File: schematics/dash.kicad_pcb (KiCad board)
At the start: 2 copper layers, 50 x 30 mm, 30 parts, among them J1 BATT_CONN, J2 EXTERNAL_TRIGGER, J3 USB_OTG, SW1 SW_Push, U1 ESP-12E, U2 ch340g, U3 MCP73833, U4 HT7333, Y1 12Mhz

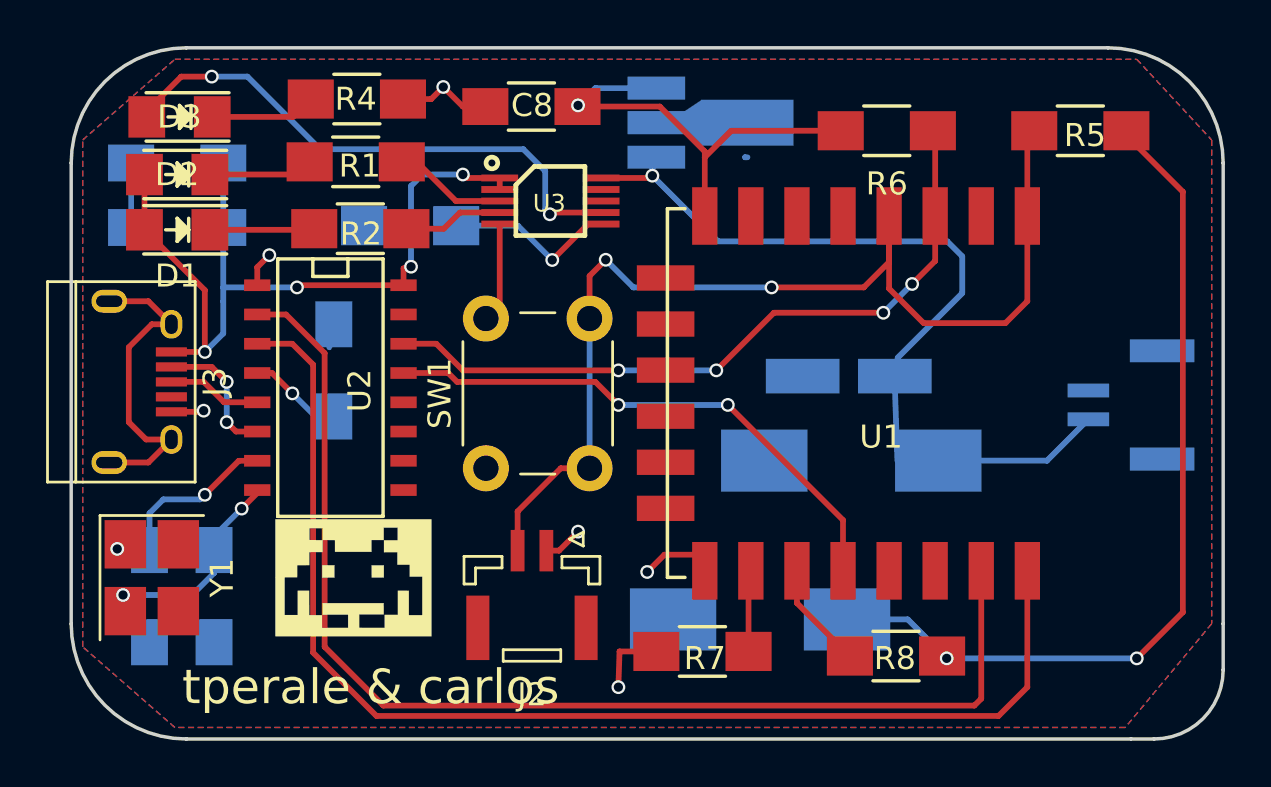
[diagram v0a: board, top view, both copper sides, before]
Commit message: [fix] Global dependencies to local dependencies (no more path problem)
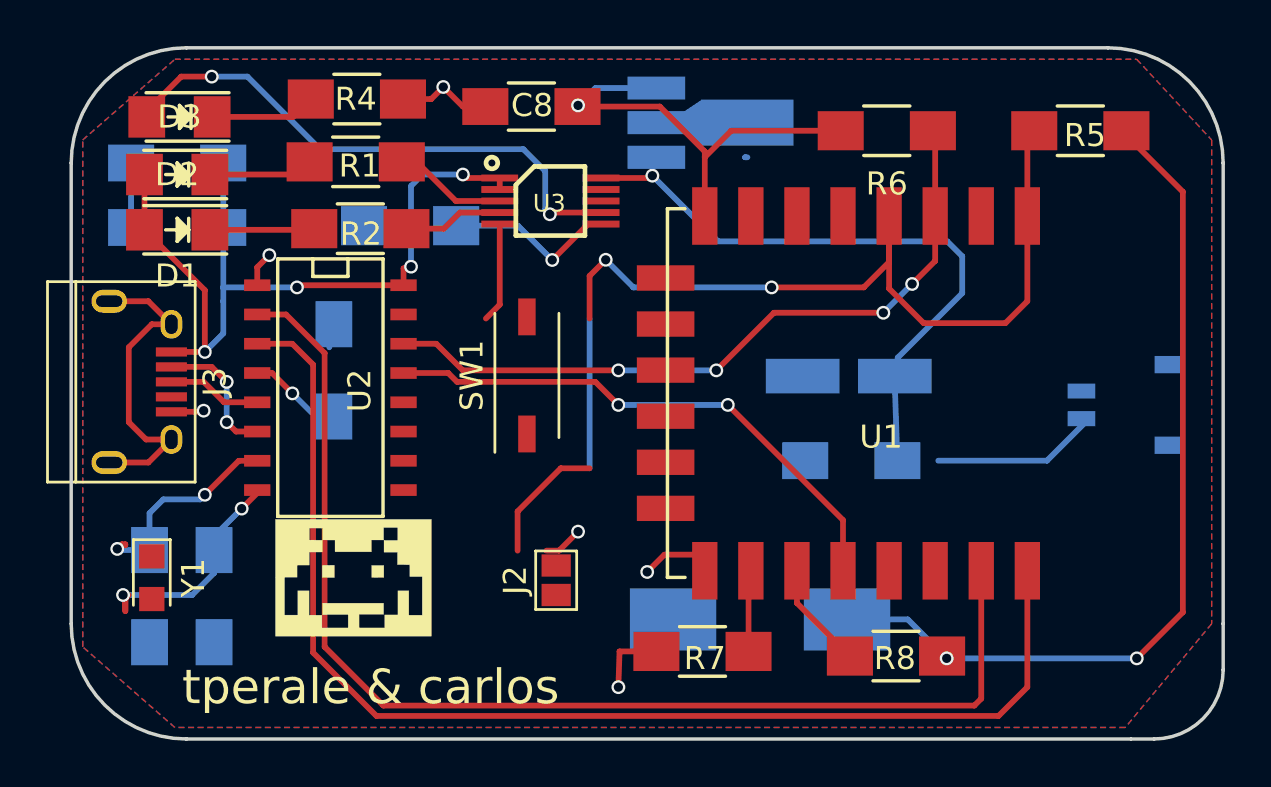
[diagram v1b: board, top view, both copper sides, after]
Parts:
- C1: footprint Capacitors_Tantalum_SMD:CP_Tantalum_Case-D_EIA-7343-31_Hand -> Capacitors_SMD:C_1206_HandSoldering
- J1: footprint Connectors_JST:JST_GH_SM02B-GHS-TB_02x1.25mm_Angled -> Connectors_JST:JST_ACH_BM02B-ACHSS_02x1.20mm_Angled
- J2: footprint Connectors_JST:JST_GH_BM02B-GHS-TBT_02x1.25mm_Straight -> Connectors:GS2
- SW1: footprint Buttons_Switches_THT:SW_PUSH_6mm -> Buttons_Switches_SMD:SW_DIP_x1_W5.08mm_Slide_Copal_CHS-A
- Y1: footprint Crystals:Crystal_SMD_3225-4pin_3.2x2.5mm_HandSoldering -> Crystals:Crystal_SMD_2012-2pin_2.0x1.2mm_HandSoldering
- moved SW1 4.41 mm to (144.8, 109.2)
- moved J2 1.12 mm to (146.1, 118.1)
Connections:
- J3 pad 4: Net-(J3-Pad4) -> (no net)
- U1 pad 13: Net-(U1-Pad13) -> (no net)
- U1 pad 14: Net-(U1-Pad14) -> (no net)
- U1 pad 17: Net-(U1-Pad17) -> (no net)
- U1 pad 18: Net-(U1-Pad18) -> (no net)
- U1 pad 19: Net-(U1-Pad19) -> (no net)
- U1 pad 2: Net-(U1-Pad2) -> (no net)
- U1 pad 20: Net-(U1-Pad20) -> (no net)
- U1 pad 21: Net-(U1-Pad21) -> (no net)
- U1 pad 22: Net-(U1-Pad22) -> (no net)
- U1 pad 5: Net-(U1-Pad5) -> (no net)
- U1 pad 6: Net-(U1-Pad6) -> (no net)
- U1 pad 7: Net-(U1-Pad7) -> (no net)
- U2 pad 10: Net-(U2-Pad10) -> (no net)
- U2 pad 11: Net-(U2-Pad11) -> (no net)
- U2 pad 12: Net-(U2-Pad12) -> (no net)
- U2 pad 15: Net-(U2-Pad15) -> (no net)
- U2 pad 9: Net-(U2-Pad9) -> (no net)
- U3 pad 8: Net-(U3-Pad8) -> (no net)
- U3 pad 9: Net-(U3-Pad9) -> (no net)
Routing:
- net (no net): track 0.10 -> 13.9 mm, vias 0 -> 1
- net /WAKE: track 46.8 -> 34.7 mm
- net GND: track 22.5 -> 20.8 mm, vias 6 -> 5

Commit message: [enh] Remove useless solder pads to have more room for the components
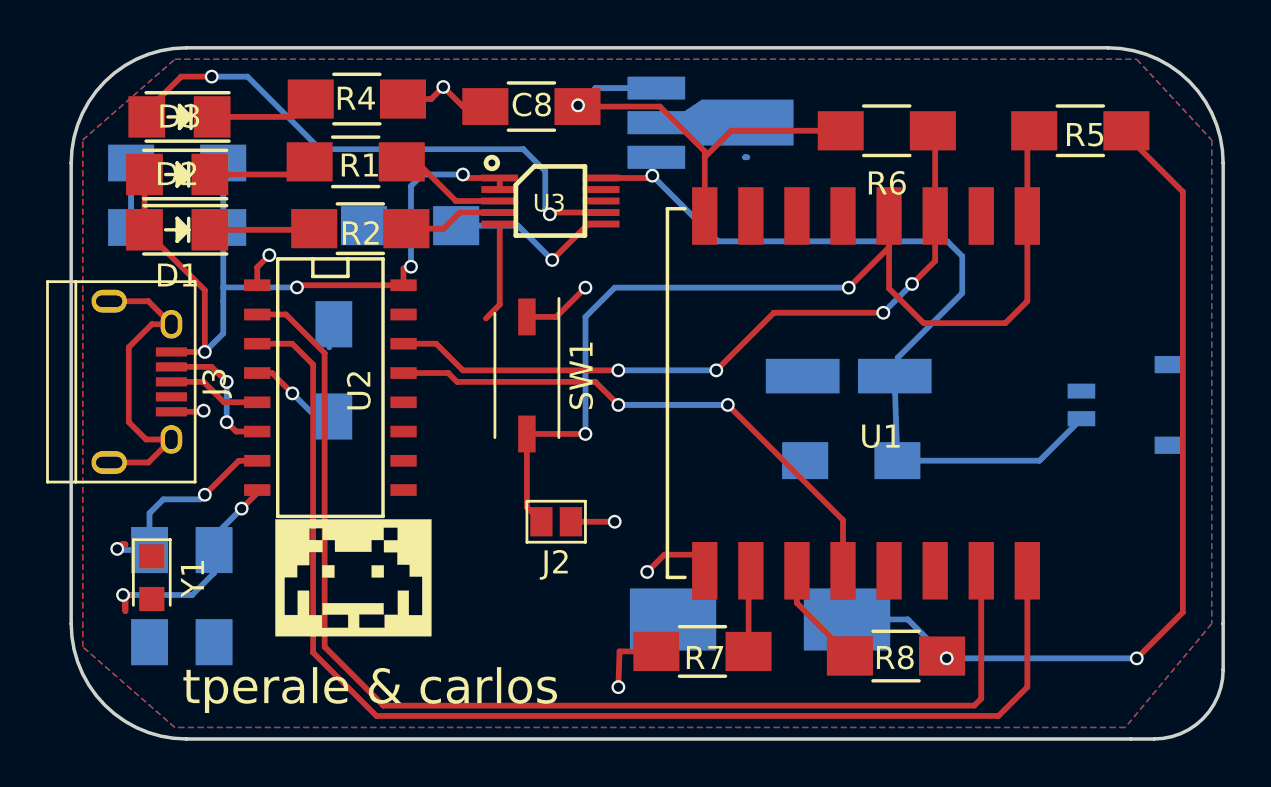
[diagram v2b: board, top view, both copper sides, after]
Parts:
- moved J2 2.54 mm to (146.1, 115.6), turned to 270 degrees
- turned SW1 to 270 degrees
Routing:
- net (no net): track 13.9 -> 0.10 mm, vias 1 -> 0
- net /WAKE: track 34.7 -> 44.1 mm
- net GND: track 20.8 -> 25.8 mm, vias 5 -> 7
- net Net-(C1-Pad1): track 35.3 -> 36.8 mm

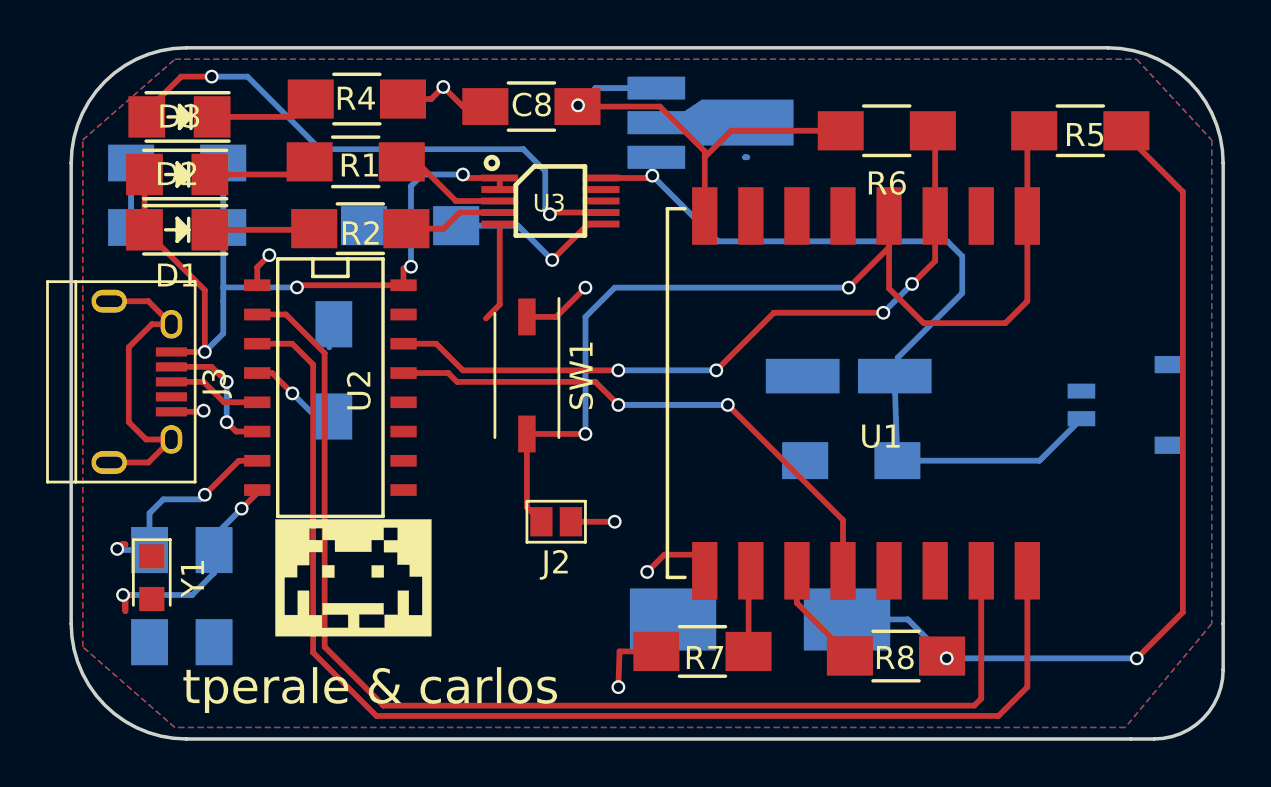
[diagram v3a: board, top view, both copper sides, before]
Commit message: [enh] Redesigned project to take less space
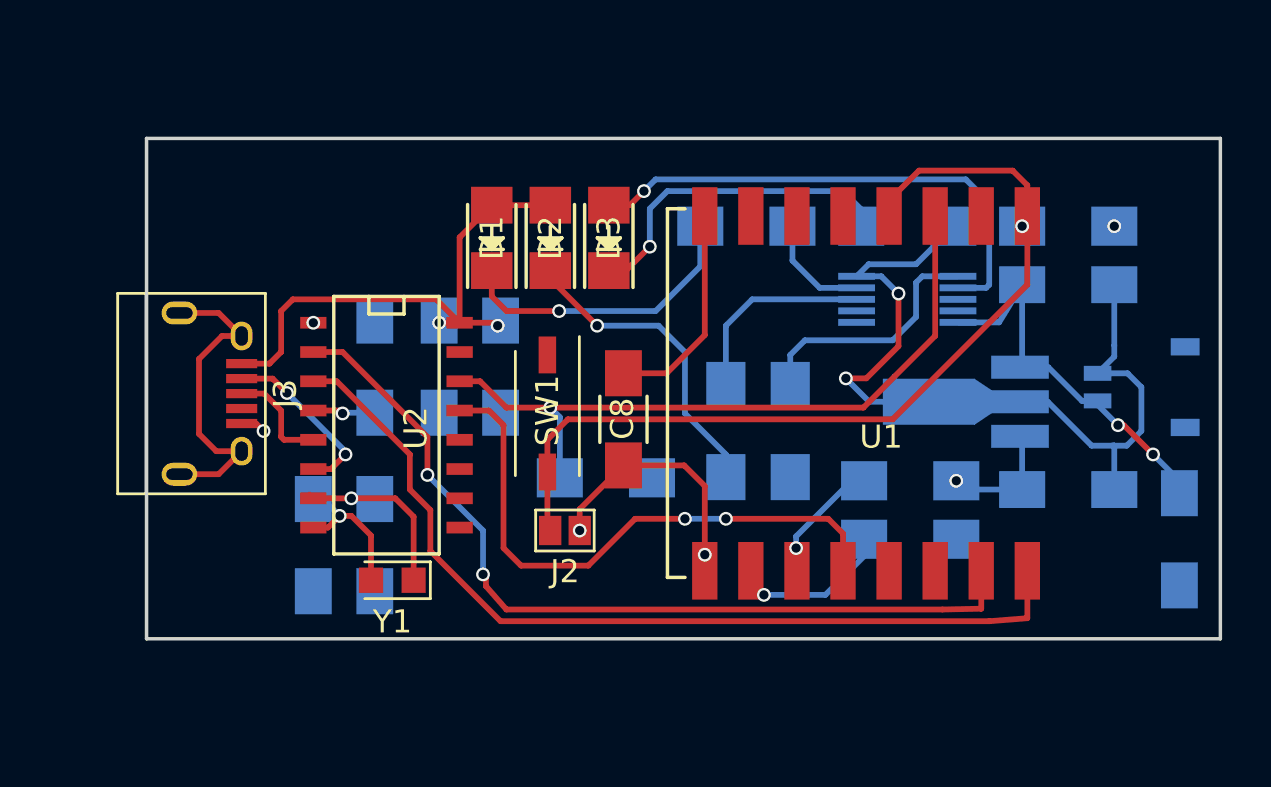
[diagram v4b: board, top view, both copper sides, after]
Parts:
- C1: value 470uF -> 220uF
- C7: footprint Capacitors_Tantalum_SMD:CP_Tantalum_Case-A_EIA-3216-18_Hand -> Capacitors_SMD:C_1206_HandSoldering
- C9: value 470uF -> 220uF; footprint Capacitors_Tantalum_SMD:CP_Tantalum_Case-D_EIA-7343-31_Hand -> Capacitors_SMD:C_1206_HandSoldering
- D1: value LED_Small -> GREEN
- D2: value LED_Small -> ORANGE
- D3: value LED -> RED
- G***, R1, R2, R4, R5, R6, R7, R8, U3: moved to B.Cu
- SW1: value SW_Push -> TRIG
- moved R4 24.5 mm to (161.3, 102.7)
- moved R1 19.9 mm to (153.4, 111.6), turned to 90 degrees
- moved R6 19.4 mm to (148.2, 113.7), turned to 0 degrees
- moved D3 19.4 mm to (148.3, 103.3), turned to 90 degrees
- moved R3 18.8 mm to (156.2, 111.6), turned to 90 degrees
- moved R2 16.8 mm to (154.3, 102.7)
- moved C5 16.6 mm to (143.6, 108.8), turned to 90 degrees
- moved D2 16.4 mm to (145.8, 103.3), turned to 90 degrees
- moved U4 16.4 mm to (163.8, 110.4), turned to 270 degrees
- moved U3 16.1 mm to (161.3, 105.9)
- moved C7 16.0 mm to (173.1, 116.3), turned to 90 degrees
- moved G*** 14.7 mm to (148.6, 108.7)
- moved C9 14.5 mm to (168.3, 114.2), turned to 0 degrees
- moved C8 14.2 mm to (149.0, 111.1), turned to 90 degrees
- moved D1 13.7 mm to (143.3, 103.3), turned to 90 degrees
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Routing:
- net +3V3: track 59.7 -> 15.6 mm, vias 3 -> 2
- net GND: track 25.8 -> 46.2 mm, vias 7 -> 6
- net Net-(C1-Pad1): track 36.8 -> 17.0 mm, vias 1 -> 2
- net /TXD: track 54.2 -> 40.0 mm
- net /RXD: track 52.3 -> 38.3 mm, vias 0 -> 2
- net +5V: track 35.6 -> 23.3 mm, vias 4 -> 2
- net Net-(D3-Pad1): track 4.60 -> 14.4 mm, vias 0 -> 1
- net Net-(D2-Pad1): track 4.56 -> 14.3 mm, vias 0 -> 1
- net Net-(D1-Pad1): track 4.55 -> 13.0 mm, vias 0 -> 1
- net Net-(C3-Pad1): track 10.9 -> 6.67 mm, vias 2 -> 1
- net Net-(R1-Pad2): track 4.95 -> 8.72 mm
- net Net-(R3-Pad2): track 7.55 -> 11.1 mm, vias 1 -> 0
- net /GPIO15: track 4.38 -> 7.90 mm, vias 0 -> 1
- net /WAKE: track 44.1 -> 41.7 mm, vias 2 -> 1
- net /D-: track 5.70 -> 7.61 mm
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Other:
- board size 50 x 30 mm -> 46.6 x 21.7 mm

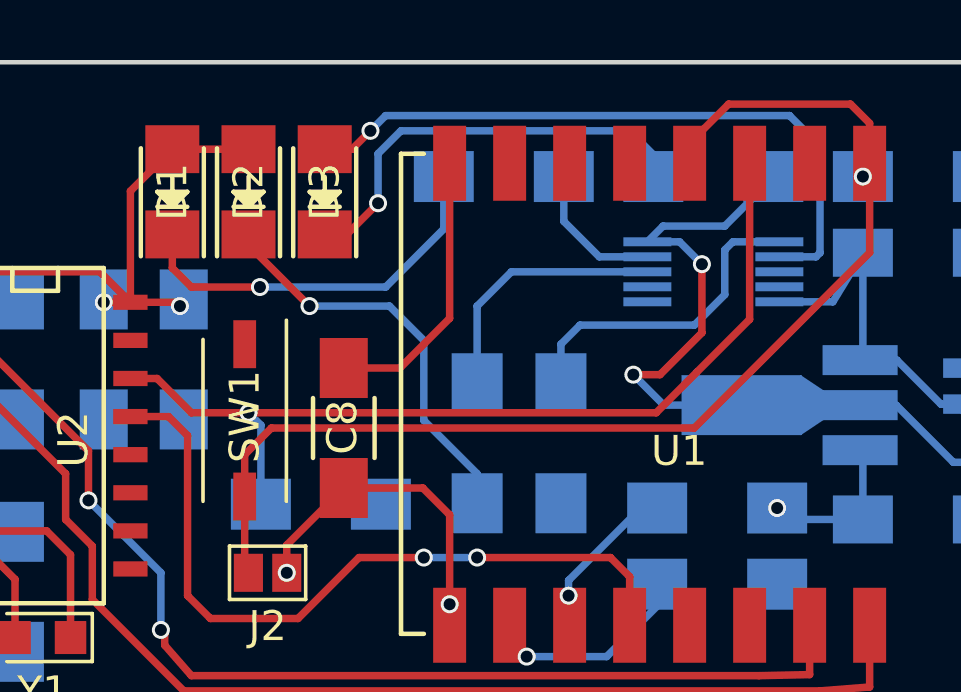
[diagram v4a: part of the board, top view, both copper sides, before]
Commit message: [fix] unconnected
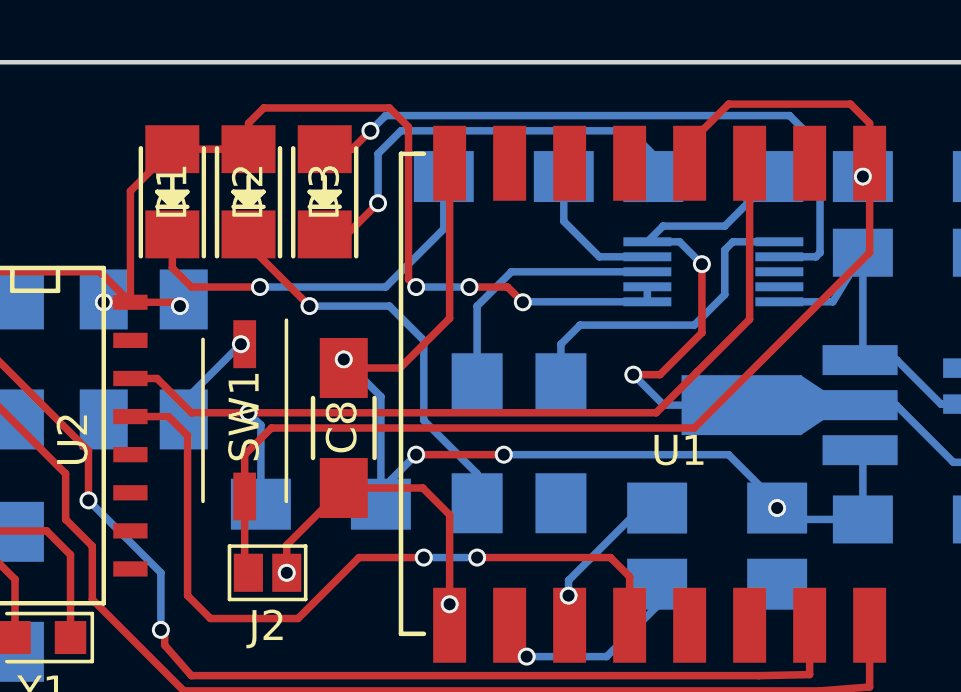
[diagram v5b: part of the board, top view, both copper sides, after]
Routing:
- net +3V3: track 15.6 -> 36.2 mm, vias 2 -> 5
- net +5V: track 23.3 -> 43.8 mm, vias 2 -> 5
- net GND: track 46.2 -> 49.6 mm, vias 6 -> 7
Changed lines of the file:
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@@
   (general
     (links 66)
-    (no_connects 5)
+    (no_connects 0)
     (area 128.194999 98.857999 174.954001 120.725001)
     (thickness 1.6)
     (drawings 5)
-    (tracks 257)
+    (tracks 288)
     (zones 0)
     (modules 30)
@@
   (segment (start 166.275 105.283) (end 166.275 108.7689) (width 0.25) (layer B.Cu) (net 1) (status 20))
   (segment (start 166.275 108.7689) (end 166.18204 108.86186) (width 0.25) (layer B.Cu) (net 1) (status 30))
+  (segment (start 143.637 110.839) (end 143.637 110.236) (width 0.25) (layer B.Cu) (net 2))
+  (segment (start 143.637 110.236) (end 145.542 108.331) (width 0.25) (layer B.Cu) (net 2))
+  (via (at 145.542 108.331) (size 0.6) (drill 0.4) (layers F.Cu B.Cu) (net 2))
+  (segment (start 145.542 108.331) (end 145.669 108.331) (width 0.25) (layer F.Cu) (net 2))
   (segment (start 166.18204 110.363) (end 167.386 110.363) (width 0.25) (layer B.Cu) (net 2))
   (segment (start 167.386 110.363) (end 169.291 112.268) (width 0.25) (layer B.Cu) (net 2))
@@
   (segment (start 139.7 112.649) (end 139.7 114.173) (width 0.25) (layer F.Cu) (net 21))
   (segment (start 136.525 109.474) (end 139.7 112.649) (width 0.25) (layer F.Cu) (net 21))
+  (segment (start 159.09 106.918) (end 154.956 106.918) (width 0.25) (layer B.Cu) (net 22))
+  (segment (start 145.796 100.965) (end 145.796 101.83114) (width 0.25) (layer F.Cu) (net 22))
+  (segment (start 146.304 100.457) (end 145.796 100.965) (width 0.25) (layer F.Cu) (net 22))
+  (segment (start 150.495 100.457) (end 146.304 100.457) (width 0.25) (layer F.Cu) (net 22))
+  (segment (start 151.13 101.092) (end 150.495 100.457) (width 0.25) (layer F.Cu) (net 22))
+  (segment (start 151.13 106.172) (end 151.13 101.092) (width 0.25) (layer F.Cu) (net 22))
+  (segment (start 151.384 106.426) (end 151.13 106.172) (width 0.25) (layer F.Cu) (net 22))
+  (via (at 151.384 106.426) (size 0.6) (drill 0.4) (layers F.Cu B.Cu) (net 22))
+  (segment (start 153.162 106.426) (end 151.384 106.426) (width 0.25) (layer B.Cu) (net 22))
+  (via (at 153.162 106.426) (size 0.6) (drill 0.4) (layers F.Cu B.Cu) (net 22))
+  (segment (start 154.432 106.426) (end 153.162 106.426) (width 0.25) (layer F.Cu) (net 22))
+  (segment (start 154.94 106.934) (end 154.432 106.426) (width 0.25) (layer F.Cu) (net 22))
+  (via (at 154.94 106.934) (size 0.6) (drill 0.4) (layers F.Cu B.Cu) (net 22))
+  (segment (start 154.956 106.918) (end 154.94 106.934) (width 0.25) (layer B.Cu) (net 22))
+  (segment (start 159.09 106.418) (end 159.09 106.918) (width 0.25) (layer B.Cu) (net 22))
   (segment (start 143.256 101.83114) (end 145.796 101.83114) (width 0.25) (layer F.Cu) (net 22))
   (segment (start 141.859 106.934) (end 141.859 103.22814) (width 0.25) (layer F.Cu) (net 22))
@@
   (segment (start 140.97 106.934) (end 140.97 106.839) (width 0.25) (layer B.Cu) (net 22))
   (via (at 140.97 106.934) (size 0.6) (drill 0.4) (layers F.Cu B.Cu) (net 22))
+  (segment (start 150.209 113.665) (end 150.209 113.189) (width 0.25) (layer B.Cu) (net 23))
+  (segment (start 150.209 113.189) (end 151.384 112.014) (width 0.25) (layer B.Cu) (net 23))
+  (segment (start 161.798 112.014) (end 163.417 113.633) (width 0.25) (layer B.Cu) (net 23))
+  (segment (start 154.305 112.014) (end 161.798 112.014) (width 0.25) (layer B.Cu) (net 23))
+  (via (at 154.305 112.014) (size 0.6) (drill 0.4) (layers F.Cu B.Cu) (net 23))
+  (segment (start 151.384 112.014) (end 154.305 112.014) (width 0.25) (layer F.Cu) (net 23))
+  (via (at 151.384 112.014) (size 0.6) (drill 0.4) (layers F.Cu B.Cu) (net 23))
+  (segment (start 163.417 113.633) (end 163.417 113.792) (width 0.25) (layer B.Cu) (net 23))
+  (segment (start 150.209 113.665) (end 150.209 110.077) (width 0.25) (layer B.Cu) (net 23))
+  (segment (start 148.971 108.839) (end 148.971 109.125) (width 0.25) (layer F.Cu) (net 23))
+  (via (at 148.971 108.839) (size 0.6) (drill 0.4) (layers F.Cu B.Cu) (net 23))
+  (segment (start 150.209 110.077) (end 148.971 108.839) (width 0.25) (layer B.Cu) (net 23))
   (via (at 170.275 102.743) (size 0.6) (drill 0.4) (layers F.Cu B.Cu) (net 23))
   (segment (start 170.275 102.743) (end 170.307 102.743) (width 0.25) (layer F.Cu) (net 23))
